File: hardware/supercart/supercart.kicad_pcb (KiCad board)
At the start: 2 copper layers, 58 x 60 mm, 7 parts, among them J1 C64_EDGE_CONNECTOR_44, U1 ATF22V10C_SUPERCART, U2 AM29F080B_SO44

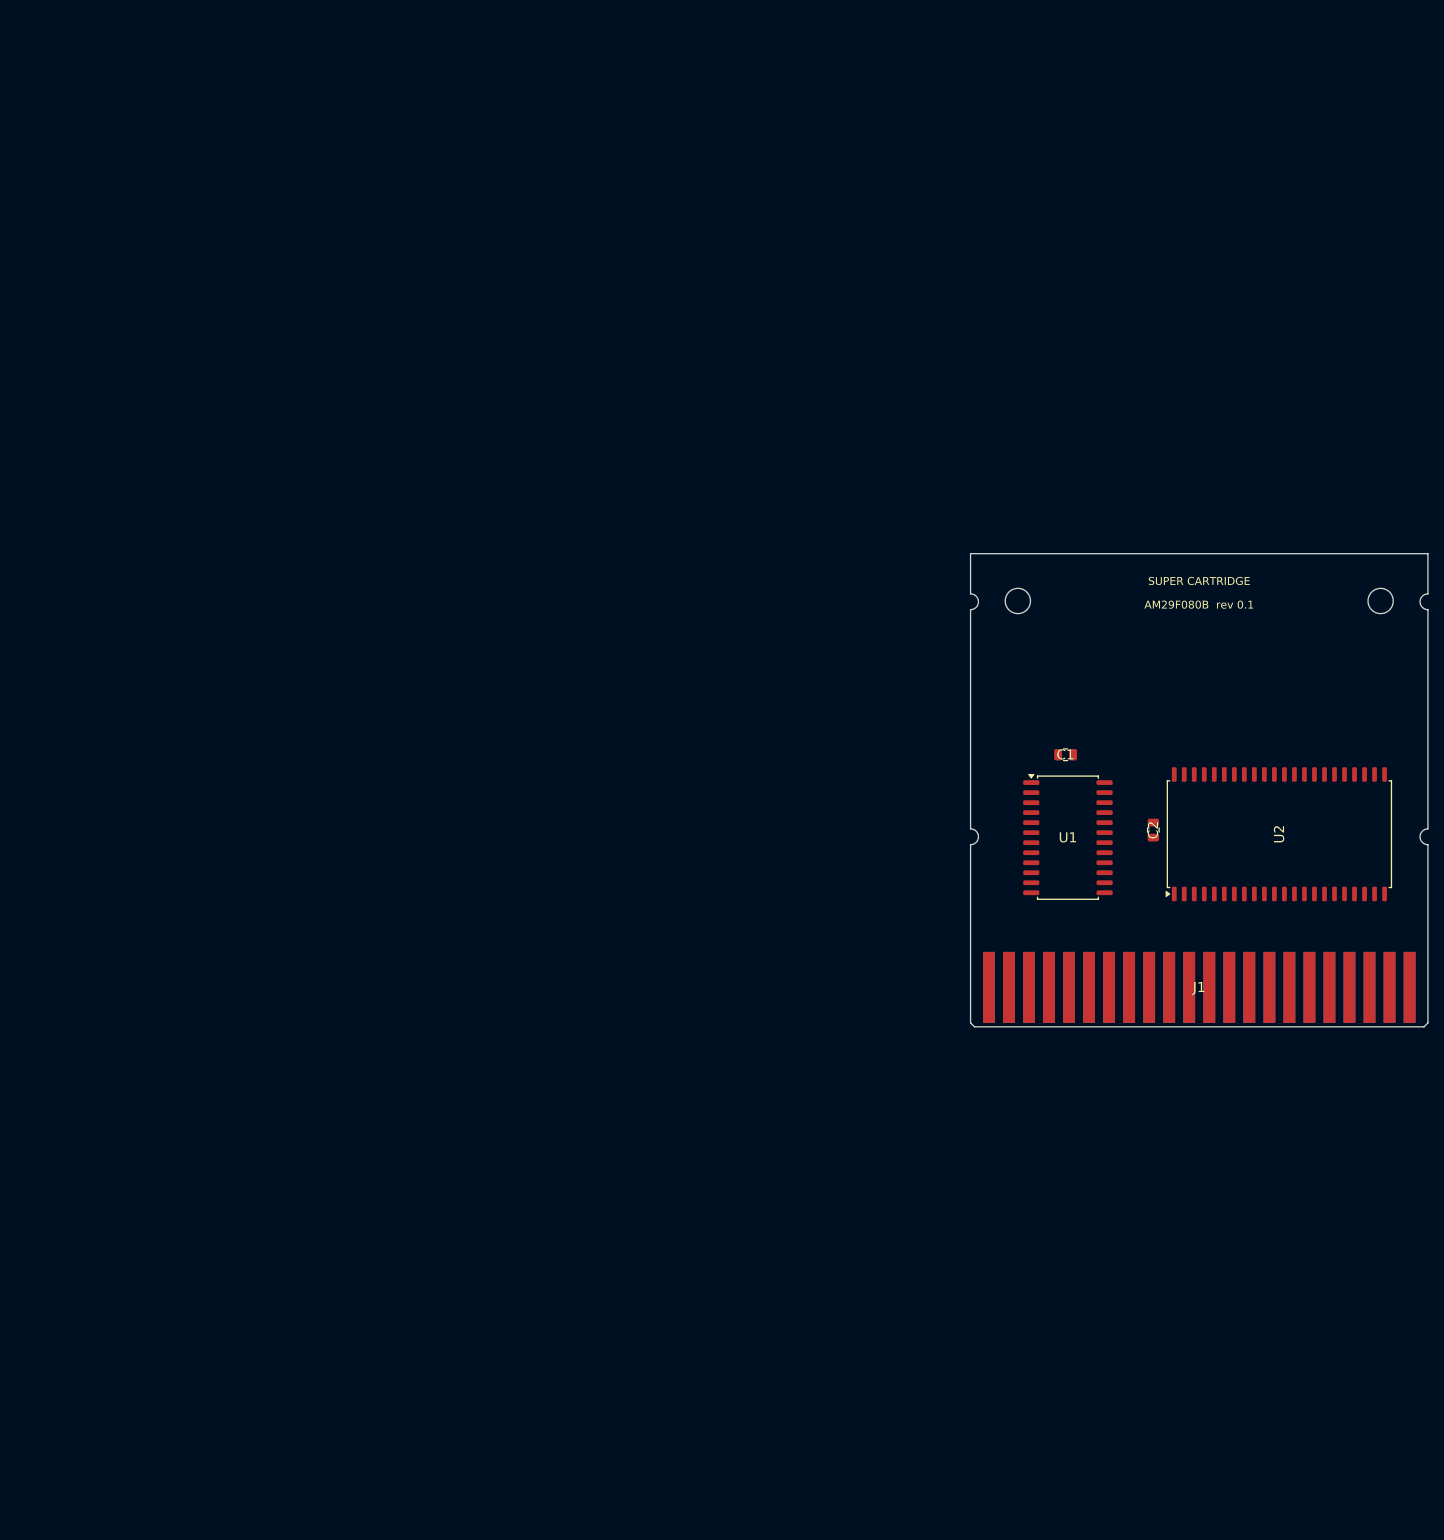
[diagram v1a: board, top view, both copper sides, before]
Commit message: Fix U2/J1 KiCad footprint bugs, verify all pinouts, add PINOUTS reference
U2 (AM29F080B): the "horizontal" footprint used a coordinate transpose
instead of a true 90deg rotation, which mirrors (reverses winding of)
the pad layout rather than rotating it -- every pin ended up on the
wrong physical pad. Fixed in make_u2_horizontal_footprint.py, proven
with a shoelace-formula winding check.

J1 (C64 edge connector): numbered (1-22) and lettered (A-Z) pins had
their F.Cu/B.Cu copper-layer assignment backwards relative to a real,
verified reference cartridge (TestBoard/EpyxFastLoad.kicad_pcb). Fixed
in gen_footprints.py; not yet re-applied to the live routed PCB (would
require re-routing J1's traces -- see PINOUTS.md's "Known gap").

Added hardware/supercart/PINOUTS.md and PINOUTS.html: a consolidated,
cited pin map for U1 (ATF22V10C, verified against SUPER_CART_R01.PLD
and its own datasheet, now bundled locally), U2 (AM29F080B, ordering
code decoded as SO-44 not PSOP), and J1, plus the real bank-register/
write-arm logic and static-8K bank map. Also commits the EEPLD PLD
source, exported Gerbers, and the KiCad routing-pipeline scripts
(export_dsn/import_ses/unroute_all/fix_reference_positions) that
weren't in git yet.

Co-Authored-By: Claude Sonnet 5 <noreply@anthropic.com>
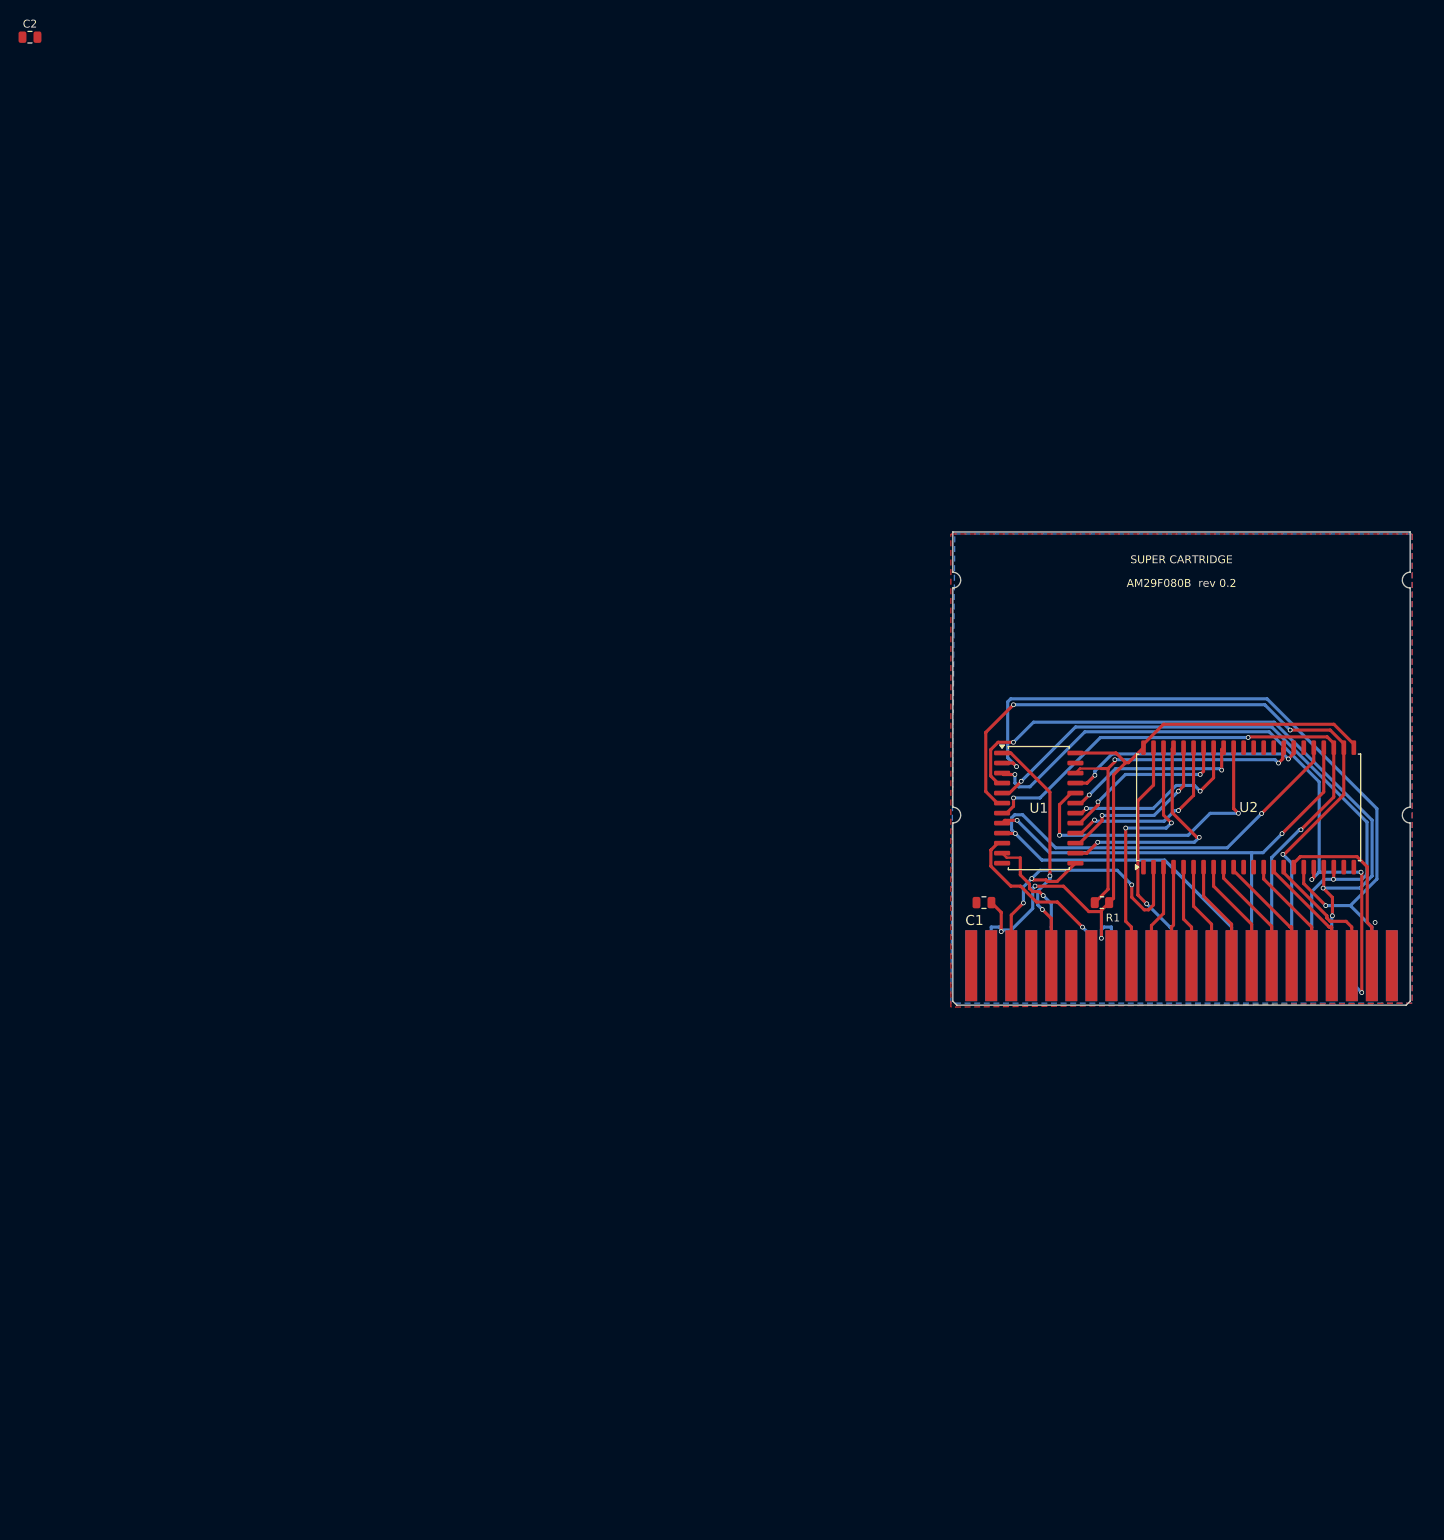
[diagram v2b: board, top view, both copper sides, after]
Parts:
- removed ? (x2): MountingHole_3.2mm_M3, MountingHole:MountingHole_3.2mm_M3
- added R1: 10k, Resistor_SMD:R_0805_2012Metric, F.Cu at (137.7, 110.8)
- U2: footprint Package_SO:SOP-44_13.3x28.2mm_P1.27mm -> supercart:SOP-44_28.2x13.3mm_P1.27mm_HORIZ
- moved C2 174.4 mm to (1.73, 1.00), turned to 0 degrees
- moved C1 21.4 mm to (122.7, 110.8)
- moved U1 5.27 mm to (129.7, 98.8)
- moved U2 5.17 mm to (156.3, 98.7), turned to 180 degrees
- moved J1 3.55 mm to (147.8, 118.8)
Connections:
- net A0 renamed /A0
- net A1 renamed /A1
- net A10 renamed /A10
- net A11 renamed /A11
- net A12 renamed /A12
- net A2 renamed /A2
- net A3 renamed /A3
- net A4 renamed /A4
- net A5 renamed /A5
- net A6 renamed /A6
- net A7 renamed /A7
- net A8 renamed /A8
- net A9 renamed /A9
- net BANK0 renamed /BANK0
- net BANK1 renamed /BANK1
- net BANK2 renamed /BANK2
- net BANK3 renamed /BANK3
- net BANK4 renamed /BANK4
- net BANK5 renamed /BANK5
- net BANK6 renamed /BANK6
- net D0 renamed /D0
- net D1 renamed /D1
- net D2 renamed /D2
- net D3 renamed /D3
- net D4 renamed /D4
- net D5 renamed /D5
- net D6 renamed /D6
- net D7 renamed /D7
- net IO1_N renamed /IO1_N
- net PHI2 renamed /PHI2
- net RESET_N renamed /RESET_N
- net RW renamed /RW
- net TBD_FLASH_RYBY_N renamed /TBD_FLASH_RYBY_N
- net TBD_ROMH_N renamed /TBD_ROMH_N
- C1 pad 1: VCC -> /VCC
- C1 pad 2: GND -> /GND
- C2 pad 1: VCC -> /VCC
- C2 pad 2: GND -> /GND
- J1 pad 1: GND -> /GND
- J1 pad 10: (no net) -> unconnected-(J1-IO2_N-Pad10)
- J1 pad 11: TBD_ROML_N -> /ROML_N
- J1 pad 12: (no net) -> unconnected-(J1-BA-Pad12)
- J1 pad 13: (no net) -> unconnected-(J1-DMA_N-Pad13)
- J1 pad 2: VCC -> /VCC
- J1 pad 22: GND -> /GND
- J1 pad 3: VCC -> /VCC
- J1 pad 4: (no net) -> unconnected-(J1-IRQ_N-Pad4)
- J1 pad 6: (no net) -> unconnected-(J1-DOTCLK-Pad6)
- J1 pad 8: TBD_GAME_N -> /VCC
- J1 pad 9: TBD_EXROM_N -> /GND
- J1 pad A: GND -> /GND
- J1 pad D: (no net) -> unconnected-(J1-NMI_N-PadD)
- J1 pad F: (no net) -> unconnected-(J1-A15-PadF)
- J1 pad H: (no net) -> unconnected-(J1-A14-PadH)
- J1 pad J: (no net) -> unconnected-(J1-A13-PadJ)
- J1 pad Z: GND -> /GND
- U1 pad 12: GND -> /GND
- U1 pad 21: TBD_CTRL0 -> /FLASH_OE_N
- U1 pad 22: TBD_CTRL1_FLASH_WRITE_SAFETY -> /FLASH_WE_N
- U1 pad 23: TBD_CTRL2 -> unconnected-(U1-CTRL2-Pad23)
- U1 pad 24: VCC -> /VCC
- U2 pad 1: (no net) -> unconnected-(U2-NC-Pad1)
- U2 pad 11: (no net) -> unconnected-(U2-NC-Pad11)
- U2 pad 12: (no net) -> unconnected-(U2-NC-Pad12)
- U2 pad 21: GND -> /GND
- U2 pad 22: GND -> /GND
- U2 pad 23: VCC -> /VCC
- U2 pad 29: TBD_FLASH_OE_N -> /FLASH_OE_N
- U2 pad 30: TBD_FLASH_WE_N -> /FLASH_WE_N
- U2 pad 31: (no net) -> unconnected-(U2-NC-Pad31)
- U2 pad 32: (no net) -> unconnected-(U2-NC-Pad32)
- U2 pad 33: (no net) -> unconnected-(U2-NC-Pad33)
- U2 pad 34: (no net) -> unconnected-(U2-NC-Pad34)
- U2 pad 43: TBD_FLASH_CE_N -> /ROML_N
- U2 pad 44: VCC -> /VCC
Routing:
- net /VCC: track 0.00 -> 103.7 mm, vias 0 -> 3
- net /D0: track 0.00 -> 95.0 mm, vias 0 -> 2
- net /D4: track 0.00 -> 91.0 mm, vias 0 -> 3
- net /D7: track 0.00 -> 87.6 mm, vias 0 -> 2
- net /D2: track 0.00 -> 87.1 mm, vias 0 -> 3
- net /D1: track 0.00 -> 86.1 mm, vias 0 -> 4
- net /D3: track 0.00 -> 80.2 mm, vias 0 -> 2
- net /D5: track 0.00 -> 78.6 mm, vias 0 -> 3
- net /D6: track 0.00 -> 65.8 mm, vias 0 -> 2
- net /FLASH_WE_N: track 0.00 -> 46.7 mm, vias 0 -> 2
- net /RESET_N: track 0.00 -> 42.7 mm, vias 0 -> 3
- net /BANK6: track 0.00 -> 38.9 mm, vias 0 -> 2
- net /A12: track 0.00 -> 33.8 mm, vias 0 -> 2
- net /PHI2: track 0.00 -> 31.5 mm, vias 0 -> 2
- net /FLASH_OE_N: track 0.00 -> 30.8 mm, vias 0 -> 2
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- added copper zone on B.Cu, net /GND
- added copper zone on F.Cu, net /GND
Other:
- board text added: "AM29F080B rev 0.2"
- board text removed: "AM29F080B rev 0.1"
